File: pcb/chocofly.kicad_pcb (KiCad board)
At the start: 2 copper layers, 304 x 133.5 mm, 193 parts, among them P1 battery+, P2 battery-, SW1 SW_Push, SW11 SW_Push, SW12 SW_Push, SW13 SW_Push, SW14 SW_Push, SW15 SW_Push, SW16 SW_Push, SW17 SW_Push, SW18 SW_Push, SW19 SW_Push, SW2 SW_Push, SW20 SW_Push, SW21 SW_Push, SW22 SW_Push, SW23 SW_Push, SW24 SW_Push, SW25 SW_Push, SW26 SW_Push, SW27 SW_Push, SW28 SW_Push, SW29 SW_Push, SW3 SW_Push, SW30 SW_Push, SW31 SW_Push, SW32 SW_Push, SW33 SW_Push, SW34 SW_Push, SW35 SW_Push, SW36 SW_Push, SW37 SW_Push, SW38 SW_Push, SW39 SW_Push, SW4 SW_Push, SW40 SW_Push, SW41 SW_Push, SW42 SW_Push, SW43 SW_Push, SW44 SW_Push, SW45 SW_Push, SW46 SW_Push, SW47 SW_Push, SW48 SW_Push, SW49 SW_Push, SW5 SW_Push, SW50 SW_Push, SW51 SW_Push, SW52 SW_Push, SW53 SW_Push, SW54 SW_Push, SW55 SW_Push, SW56 SW_Push, SW57 SW_Push, SW58 SW_Push, SW59 SW_Push, SW6 SW_Push, SW60 SW_Push, SW61 SW_Push, SW62 Reset, SW63 Power, SW64 Power, SW7 SW_Push, SW8 SW_Push, SW9 SW_Push

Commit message: wiring in progress
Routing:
- net col0: track 53.4 -> 122.9 mm
- net Net-(D7-A): track 0.00 -> 22.4 mm
- net Net-(D30-A): track 0.00 -> 21.9 mm
- net Net-(D14-A): track 0.00 -> 21.9 mm
- net Net-(D46-A): track 0.00 -> 21.8 mm
- net Net-(D1-A): track 0.00 -> 21.7 mm
- net row3: track 164.1 -> 147.9 mm
- net Net-(D6-A): track 0.00 -> 9.86 mm
- net encB: track 76.3 -> 67.1 mm
- net Net-(D3-A): track 0.00 -> 9.16 mm
- net Net-(D8-A): track 0.00 -> 9.14 mm
- net Net-(D51-A): track 0.00 -> 9.10 mm
- net Net-(D50-A): track 0.00 -> 9.09 mm
- net Net-(D12-A): track 0.00 -> 9.09 mm
- net Net-(D15-A): track 0.00 -> 9.08 mm
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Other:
- outline, holes or cut-outs redrawn

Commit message: wip
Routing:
- net Net-(D9-A): track 9.05 -> 22.9 mm
- net Net-(D4-A): track 8.99 -> 22.7 mm
- net Net-(D5-A): track 9.00 -> 22.4 mm
- net Net-(D11-A): track 9.01 -> 22.4 mm
- net Net-(D3-A): track 9.16 -> 22.5 mm
- net Net-(D2-A): track 9.05 -> 22.4 mm
- net Net-(D13-A): track 9.00 -> 22.3 mm
- net Net-(D6-A): track 9.86 -> 22.9 mm
- net Net-(D34-A): track 8.99 -> 22.0 mm
- net Net-(D43-A): track 9.06 -> 22.0 mm
- net Net-(D27-A): track 8.98 -> 21.9 mm
- net Net-(D42-A): track 9.00 -> 22.0 mm
- net Net-(D26-A): track 9.01 -> 22.0 mm
- net Net-(D44-A): track 9.07 -> 22.0 mm
- net Net-(D33-A): track 8.99 -> 21.9 mm
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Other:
- outline, holes or cut-outs redrawn

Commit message: wip
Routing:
- net col2: track 50.5 -> 304.8 mm
- net col1: track 52.0 -> 296.4 mm
- net col3: track 51.9 -> 229.5 mm
- net row4: track 124.2 -> 283.3 mm, vias 5 -> 6
- net row2: track 153.3 -> 307.9 mm, vias 5 -> 6
- net col0: track 122.9 -> 275.3 mm
- net row6: track 92.6 -> 240.3 mm
- net row3: track 147.9 -> 287.5 mm
- net row7: track 86.4 -> 223.8 mm
- net row5: track 121.3 -> 254.0 mm
- net row0: track 110.4 -> 225.6 mm
- net row1: track 173.3 -> 268.8 mm

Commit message: routing wip
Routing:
- net col4: track 49.3 -> 240.1 mm
- net row4: track 283.3 -> 465.4 mm
- net row6: track 240.3 -> 398.6 mm
- net row2: track 307.9 -> 463.8 mm
- net row0: track 225.6 -> 378.9 mm
- net row5: track 254.0 -> 406.9 mm
- net row3: track 287.5 -> 428.7 mm, vias 7 -> 8
- net row7: track 223.8 -> 353.5 mm
- net row1: track 268.8 -> 387.9 mm, vias 6 -> 7
- net Net-(D50-A): track 9.09 -> 22.0 mm
- net Net-(MCU1-RST): track 9.64 -> 16.1 mm
- net GND: track 125.5 -> 119.8 mm
- net encB: track 67.1 -> 70.8 mm
- net col0: track 275.3 -> 274.0 mm
- net encA: track 72.8 -> 73.6 mm, vias 1 -> 2
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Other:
- outline, holes or cut-outs redrawn

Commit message: wip
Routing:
- net col7: track 44.2 -> 276.9 mm
- net col5: track 42.7 -> 274.1 mm
- net col6: track 46.4 -> 270.3 mm
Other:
- outline, holes or cut-outs redrawn

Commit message: checks ok
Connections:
- ENC1 pad A: Net-(ENC1-PadA) -> encA
- ENC1 pad B: Net-(ENC1-PadB) -> encB
- JP1 pad 1: Net-(ENC1-PadA) -> encA
- JP2 pad 1: Net-(ENC1-PadB) -> encB
- SW63 pad 3: Net-(SW63A-C) -> Net-(P1-Pin_1)
- SW64 pad 2: Net-(SW63A-C) -> Net-(MCU1-RAW)
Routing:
- net col7: track 276.9 -> 393.5 mm
- net col6: track 270.3 -> 349.5 mm, vias 2 -> 3
- net col0: track 274.0 -> 332.8 mm, vias 2 -> 0
- net encA: track 73.6 -> 124.1 mm, vias 2 -> 3
- net col5: track 274.1 -> 316.1 mm
- net encB: track 70.8 -> 110.3 mm, vias 1 -> 3
- net col2: track 304.8 -> 334.6 mm, vias 2 -> 3
- net col1: track 295.9 -> 318.0 mm, vias 2 -> 0
- net GND: track 119.8 -> 135.2 mm
- net Net-(ENC2-PadA): track 0.00 -> 11.7 mm
- net Net-(ENC2-PadB): track 0.00 -> 10.9 mm
- net Net-(MCU1-RAW): track 40.6 -> 50.7 mm, vias 0 -> 2
- net Net-(P1-Pin_1): track 23.0 -> 31.9 mm, vias 1 -> 2
- net row3: track 428.7 -> 420.5 mm
- net row7: track 353.5 -> 349.7 mm, vias 2 -> 1
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
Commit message: fix
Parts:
- removed H1, H17, H20, H30, H31, H32, H33, H34, H35, H4, H5, H6: 5mm, footprints:hole_5mm
- removed H10, H11, H12, H15, H16, H18, H42, H43, H46, H9: 2mm, footprints:hole_2mm
- removed H13, H14, H48, H49, H50, H51, H67: 1mm, footprints:hole_1mm
- removed H19, H36, H37, H38, H39, H40, H41, H45, H47, H52, H53, H54, H55, H56, H57, H58, H59, H61, H62, H7, H8: 3mm, footprints:hole_3mm
- removed H2, H23, H25, H26, H27, H28, H29, H3, H44: 10mm, footprints:hole_10mm
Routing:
- net col4: track 236.6 -> 244.6 mm
- net col3: track 229.5 -> 230.1 mm

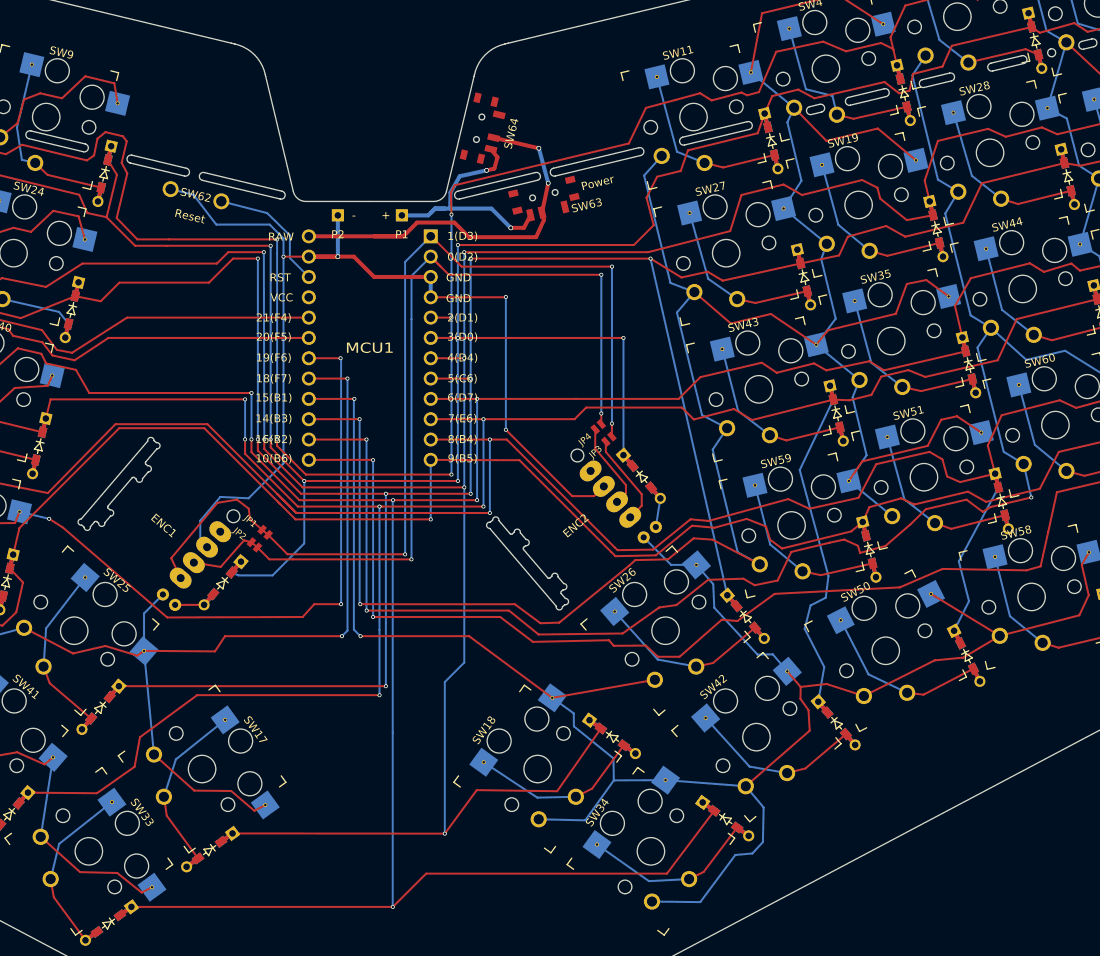
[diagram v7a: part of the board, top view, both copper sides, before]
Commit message: cleaned up tracks and vias
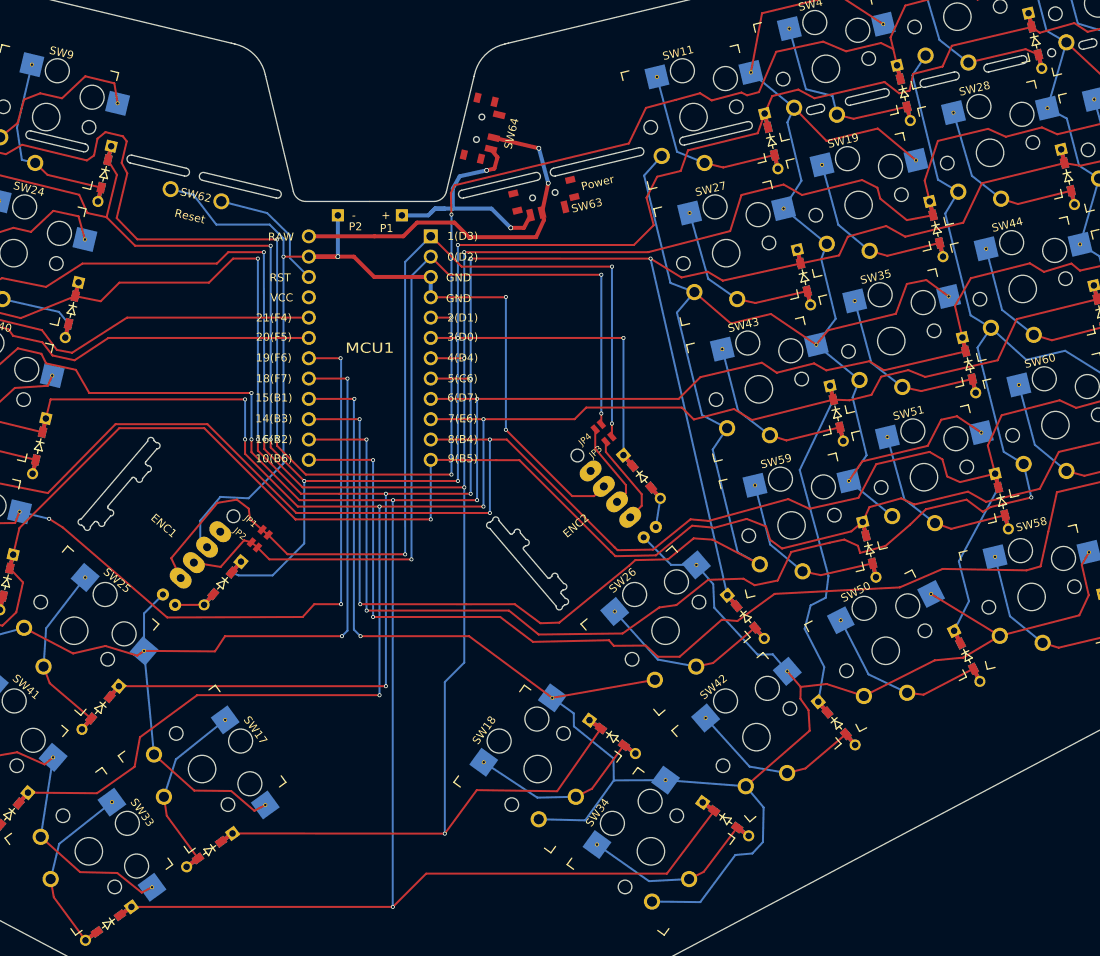
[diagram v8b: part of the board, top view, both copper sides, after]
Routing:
- net Net-(MCU1-RAW): track 50.7 -> 47.3 mm
- net row6: track 398.5 -> 395.1 mm
- net encB: track 110.3 -> 108.4 mm
- net GND: track 135.2 -> 134.0 mm
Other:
- outline, holes or cut-outs redrawn
